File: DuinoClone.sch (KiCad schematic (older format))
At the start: 13 parts, among them U1 DS1337S+, U2 24LC1025, U3 24LC1025, U4 ATMEGA328P-AU, Y1 Crystal 32MHz, Y2 Crystal 16MHz

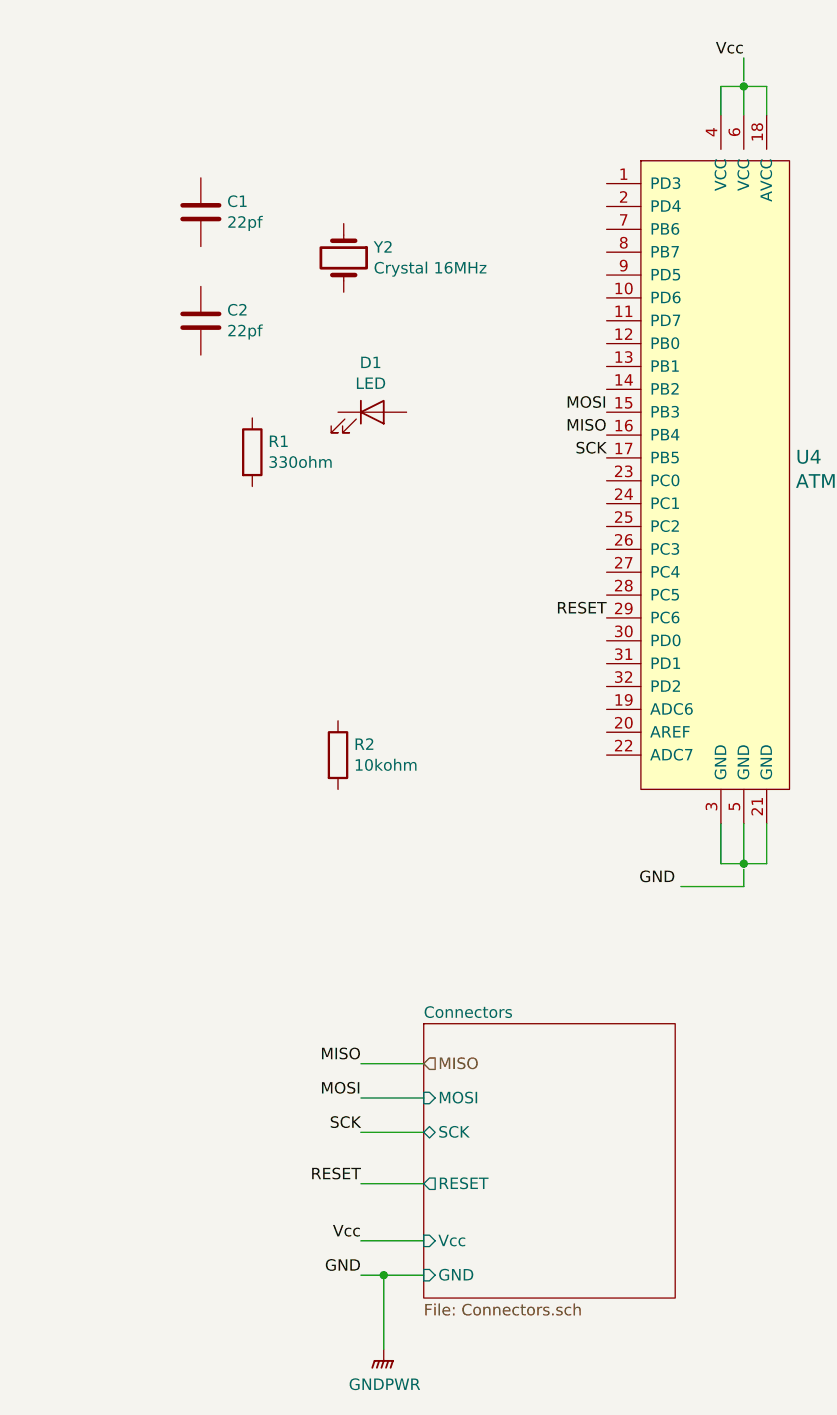
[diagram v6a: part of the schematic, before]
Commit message: Completed wiring connectors sheet
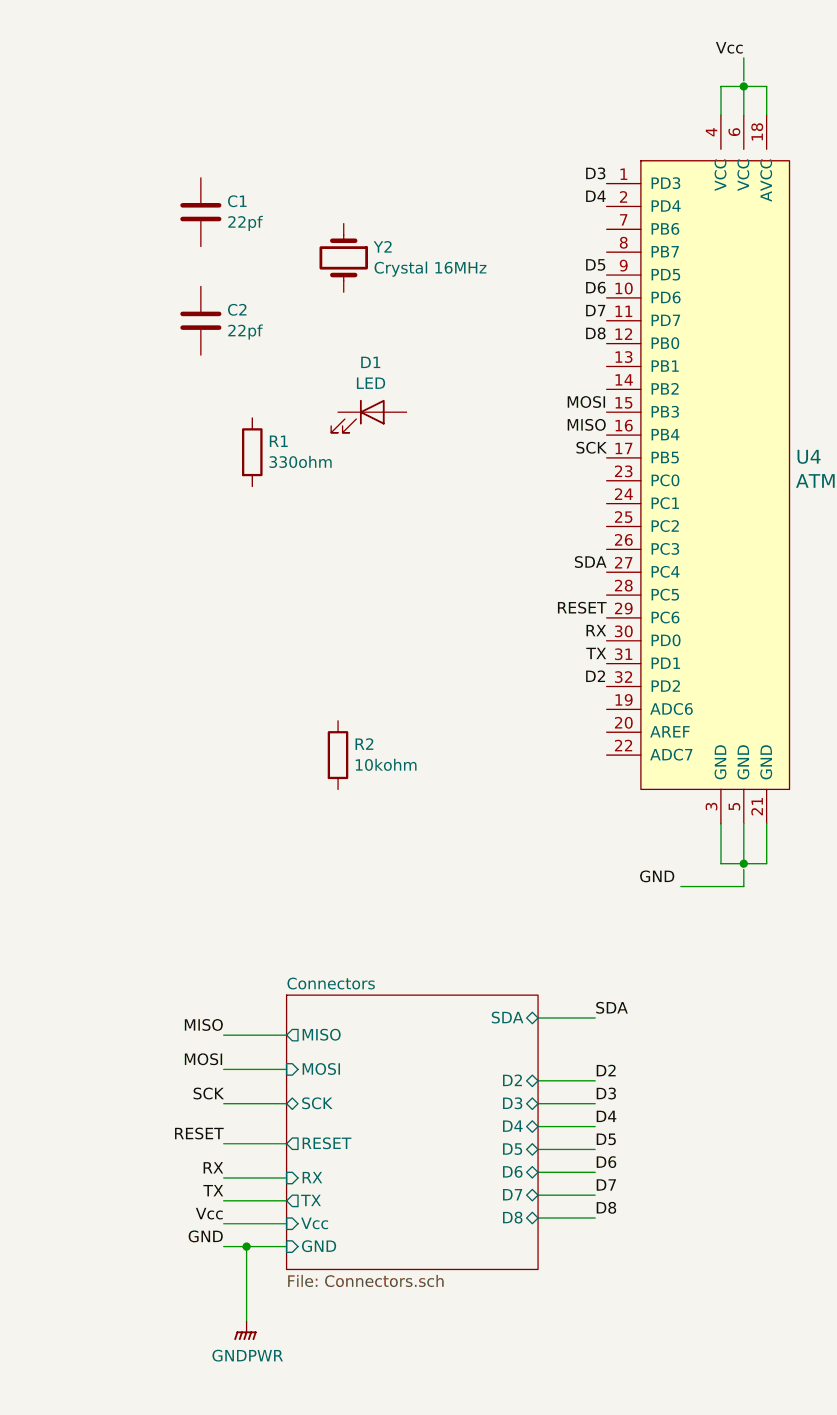
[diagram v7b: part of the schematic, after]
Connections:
- net labels added: D2, D3, D4, D5, D6, D7, D8, RX, SDA, TX
- wire segments 21 -> 31
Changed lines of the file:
@@
 	1    0    0    -1
 $EndComp
-Text HLabel 5025 6125 2    50   Input ~ 0
-MISO
-Text Label 4750 6125 2    50   ~ 0
+Text Label 4150 6000 2    50   ~ 0
 MISO
 Text Label 5825 3375 2    50   ~ 0
 MISO
 $Sheet
-S 5025 5950 1100 1200
+S 4425 5825 1100 1200
 U 5CE3C2E7
 F0 "Connectors" 50
 F1 "Connectors.sch" 50
-F2 "SCK" B L 5025 6425 50
-F3 "RESET" O L 5025 6650 50
-F4 "Vcc" I L 5025 6900 50
-F5 "MOSI" I L 5025 6275 50
-F6 "GND" I L 5025 7050 50
+F2 "SCK" B L 4425 6300 50
+F3 "RESET" O L 4425 6475 50
+F4 "Vcc" I L 4425 6825 50
+F5 "MOSI" I L 4425 6150 50
+F6 "GND" I L 4425 6925 50
+F7 "RX" I L 4425 6625 50
+F8 "TX" O L 4425 6725 50
+F9 "SDA" B R 5525 5925 50
+F10 "D2" B R 5525 6200 50
+F11 "D3" B R 5525 6300 50
+F12 "D4" B R 5525 6400 50
+F13 "D5" B R 5525 6500 50
+F14 "D6" B R 5525 6600 50
+F15 "D7" B R 5525 6700 50
+F16 "D8" B R 5525 6800 50
+F17 "MISO" O L 4425 6000 50
 $EndSheet
-Text Label 4750 6425 2    50   ~ 0
+Text Label 4150 6300 2    50   ~ 0
 SCK
-Text Label 4750 6650 2    50   ~ 0
+Text Label 4150 6475 2    50   ~ 0
 RESET
-Text Label 4750 6900 2    50   ~ 0
+Text Label 4150 6825 2    50   ~ 0
 Vcc
-Text Label 4750 6275 2    50   ~ 0
+Text Label 4150 6150 2    50   ~ 0
 MOSI
-Text Label 4750 7050 2    50   ~ 0
+Text Label 4150 6925 2    50   ~ 0
 GND
 Wire Wire Line
-	4750 6125 5025 6125
+	4150 6150 4425 6150
 Wire Wire Line
-	4750 6275 5025 6275
+	4150 6300 4425 6300
 Wire Wire Line
-	4750 6425 5025 6425
+	4150 6475 4425 6475
 Wire Wire Line
-	4750 6650 5025 6650
+	4150 6825 4425 6825
 Wire Wire Line
-	4750 6900 5025 6900
-Wire Wire Line
-	4750 7050 4850 7050
+	4150 6925 4250 6925
 Text Label 5825 3275 2    50   ~ 0
 MOSI
@@
 L power:GNDPWR #PWR?
 U 1 1 5CE88593
-P 4850 7375
-F 0 "#PWR?" H 4850 7175 50  0001 C CNN
-F 1 "GNDPWR" H 4854 7221 50  0000 C CNN
-F 2 "" H 4850 7325 50  0001 C CNN
-F 3 "" H 4850 7325 50  0001 C CNN
-	1    4850 7375
+P 4250 7250
+F 0 "#PWR?" H 4250 7050 50  0001 C CNN
+F 1 "GNDPWR" H 4254 7096 50  0000 C CNN
+F 2 "" H 4250 7200 50  0001 C CNN
+F 3 "" H 4250 7200 50  0001 C CNN
+	1    4250 7250
 	1    0    0    -1
 $EndComp
 Wire Wire Line
-	4850 7375 4850 7050
-Connection ~ 4850 7050
+	4250 7250 4250 6925
+Connection ~ 4250 6925
 Wire Wire Line
-	4850 7050 5025 7050
+	4250 6925 4425 6925
+Wire Wire Line
+	4425 6000 4150 6000
+Text Label 5775 5925 0    50   ~ 0
+SDA
+Text Label 5775 6200 0    50   ~ 0
+D2
+Text Label 5775 6300 0    50   ~ 0
+D3
+Text Label 5775 6400 0    50   ~ 0
+D4
+Text Label 5775 6500 0    50   ~ 0
+D5
+Text Label 5775 6600 0    50   ~ 0
+D6
+Text Label 5775 6700 0    50   ~ 0
+D7
+Text Label 5775 6800 0    50   ~ 0
+D8
+Text Label 4150 6625 2    50   ~ 0
+RX
+Text Label 4150 6725 2    50   ~ 0
+TX
+Wire Wire Line
+	5775 5925 5525 5925
+Wire Wire Line
+	5525 6200 5775 6200
+Wire Wire Line
+	5525 6300 5775 6300
+Wire Wire Line
+	5525 6400 5775 6400
+Wire Wire Line
+	5525 6500 5775 6500
+Wire Wire Line
+	5525 6600 5775 6600
+Wire Wire Line
+	5525 6700 5775 6700
+Wire Wire Line
+	5525 6800 5775 6800
+Wire Wire Line
+	4425 6625 4150 6625
+Wire Wire Line
+	4425 6725 4150 6725
+Text Label 5825 2275 2    50   ~ 0
+D3
+Text Label 5825 2375 2    50   ~ 0
+D4
+Text Label 5825 2675 2    50   ~ 0
+D5
+Text Label 5825 2775 2    50   ~ 0
+D6
+Text Label 5825 2875 2    50   ~ 0
+D7
+Text Label 5825 2975 2    50   ~ 0
+D8
+Text Label 5825 3975 2    50   ~ 0
+SDA
+Text Label 5825 4275 2    50   ~ 0
+RX
+Text Label 5825 4375 2    50   ~ 0
+TX
+Text Label 5825 4475 2    50   ~ 0
+D2
 $EndSCHEMATC

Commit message: Completed wiring in root sheet
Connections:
- net labels added: ADDS1, ADDS2
- wire segments 31 -> 91
- no-connect marks 0 -> 8
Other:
- moved on the sheet: BT1, C1, C2, C3, D1, R1, R2, U2, U3, Y1, Y2
